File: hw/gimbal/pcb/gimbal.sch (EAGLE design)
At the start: 80 parts, among them J1 JST-XH4SMT_RA, U1 STM32F4R_64PIN, U2 TPS62172PWSON8, U3 TPS55330PQFN16, U4 MC33926, U5 DRV8313, U6 DRV8313, U7 AS5048A

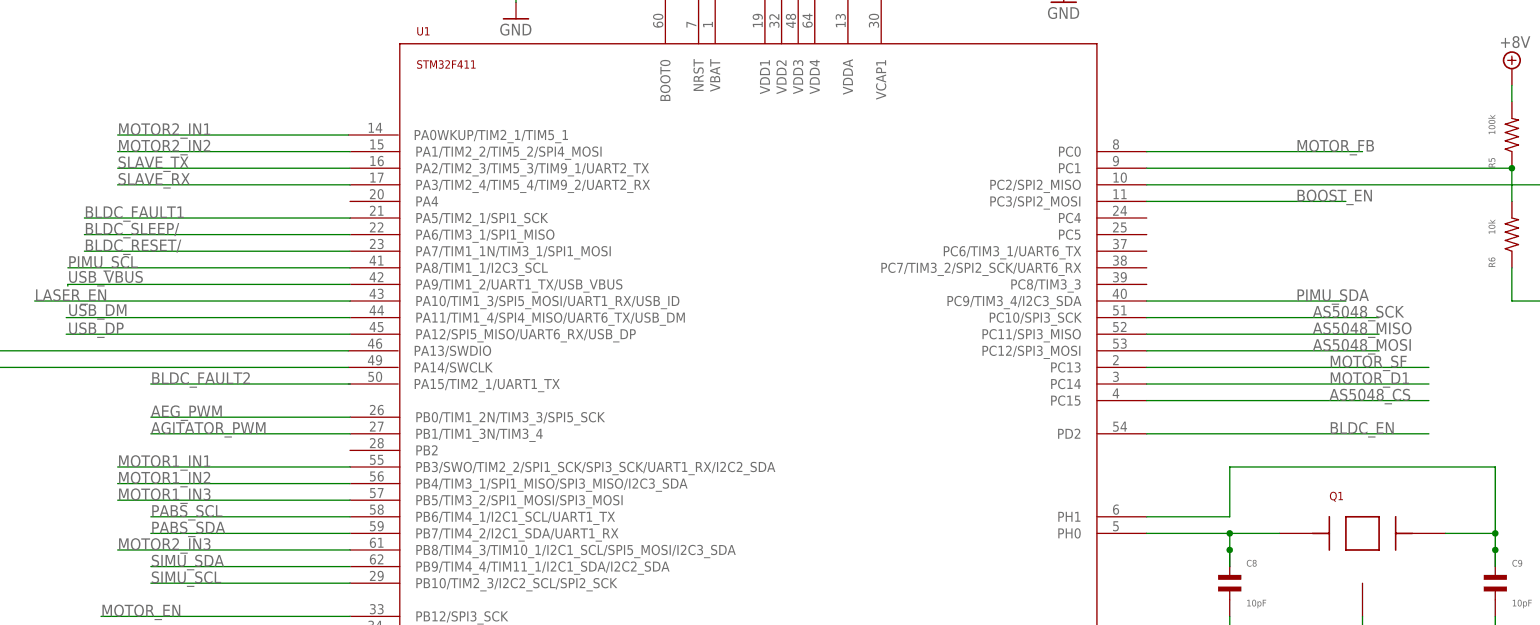
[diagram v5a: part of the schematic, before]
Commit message: gimbal: Get the board to be close to routable again, and also connect up the BLDC_FAULT2 signal, which I goofed and didn't actually connect.
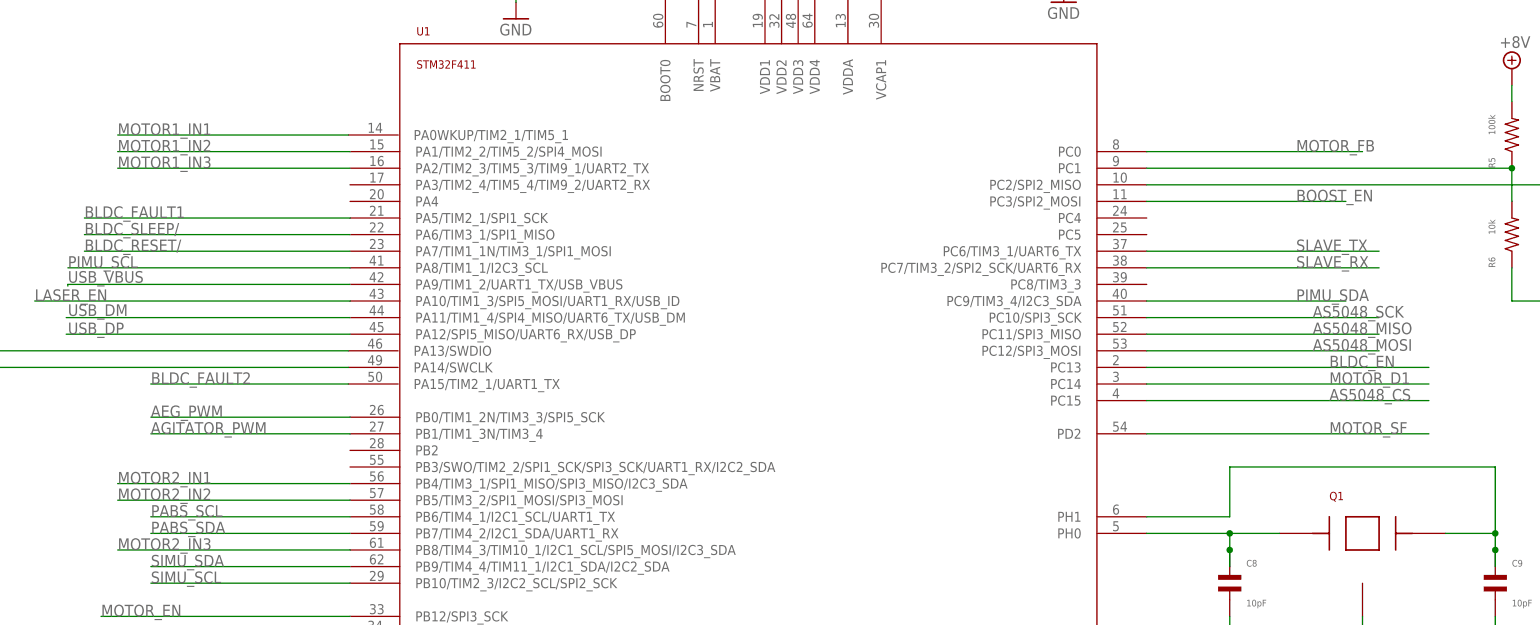
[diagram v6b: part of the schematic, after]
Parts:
- ARM: DPN 401-2002-1-ND -> 401-1999-1-ND
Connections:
- net BLDC_EN: now also U1.PC13; no longer U1.PD2
- net BLDC_FAULT2: now also U1.PA15/TIM2_1/UART1_TX
- net MOTOR1_IN1: now also U1.PA0WKUP/TIM2_1/TIM5_1; no longer U1.PB3/SWO/TIM2_2/SPI1_SCK/SPI3_SCK/UART1_RX/I2C2_SDA
- net MOTOR1_IN2: now also U1.PA1/TIM2_2/TIM5_2/SPI4_MOSI; no longer U1.PB4/TIM3_1/SPI1_MISO/SPI3_MISO/I2C3_SDA
- net MOTOR1_IN3: now also U1.PA2/TIM2_3/TIM5_3/TIM9_1/UART2_TX; no longer U1.PB5/TIM3_2/SPI1_MOSI/SPI3_MOSI
- net MOTOR2_IN1: now also U1.PB4/TIM3_1/SPI1_MISO/SPI3_MISO/I2C3_SDA; no longer U1.PA0WKUP/TIM2_1/TIM5_1
- net MOTOR2_IN2: now also U1.PB5/TIM3_2/SPI1_MOSI/SPI3_MOSI; no longer U1.PA1/TIM2_2/TIM5_2/SPI4_MOSI
- net MOTOR_SF: now also U1.PD2; no longer U1.PC13
- net SLAVE_RX: now also U1.PC7/TIM3_2/SPI2_SCK/UART6_RX; no longer U1.PA3/TIM2_4/TIM5_4/TIM9_2/UART2_RX
- net SLAVE_TX: now also U1.PC6/TIM3_1/UART6_TX; no longer U1.PA2/TIM2_3/TIM5_3/TIM9_1/UART2_TX
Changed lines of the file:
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@@
 </part>
 <part name="ARM" library="gimbal" deviceset="SLIDE_SWITCH" device="JS_SUB_SWITCH">
-<attribute name="DPN" value="401-2002-1-ND"/>
+<attribute name="DPN" value="401-1999-1-ND"/>
 </part>
 <part name="GND19" library="supply1" deviceset="GND" device=""/>
@@
 </segment>
 <segment>
-<pinref part="U1" gate="G$1" pin="PC13"/>
-<wire x1="170.18" y1="190.5" x2="213.36" y2="190.5" width="0.1524" layer="91"/>
-<label x="198.12" y="190.5" size="1.778" layer="95"/>
+<pinref part="U1" gate="G$1" pin="PD2"/>
+<wire x1="170.18" y1="180.34" x2="213.36" y2="180.34" width="0.1524" layer="91"/>
+<label x="198.12" y="180.34" size="1.778" layer="95"/>
 </segment>
 </net>
@@
 </segment>
 <segment>
-<pinref part="U1" gate="G$1" pin="PA2/TIM2_3/TIM5_3/TIM9_1/UART2_TX"/>
-<wire x1="48.26" y1="220.98" x2="12.7" y2="220.98" width="0.1524" layer="91"/>
-<label x="12.7" y="220.98" size="1.778" layer="95"/>
+<pinref part="U1" gate="G$1" pin="PC6/TIM3_1/UART6_TX"/>
+<wire x1="170.18" y1="208.28" x2="205.74" y2="208.28" width="0.1524" layer="91"/>
+<label x="193.04" y="208.28" size="1.778" layer="95"/>
 </segment>
 </net>
@@
 </segment>
 <segment>
-<pinref part="U1" gate="G$1" pin="PA3/TIM2_4/TIM5_4/TIM9_2/UART2_RX"/>
-<wire x1="48.26" y1="218.44" x2="12.7" y2="218.44" width="0.1524" layer="91"/>
-<label x="12.7" y="218.44" size="1.778" layer="95"/>
+<pinref part="U1" gate="G$1" pin="PC7/TIM3_2/SPI2_SCK/UART6_RX"/>
+<wire x1="170.18" y1="205.74" x2="205.74" y2="205.74" width="0.1524" layer="91"/>
+<label x="193.04" y="205.74" size="1.778" layer="95"/>
 </segment>
 </net>
@@
 </segment>
 <segment>
-<wire x1="48.26" y1="187.96" x2="17.78" y2="187.96" width="0.1524" layer="91"/>
+<wire x1="48.006" y1="187.96" x2="17.78" y2="187.96" width="0.1524" layer="91"/>
 <label x="17.78" y="187.96" size="1.778" layer="95"/>
+<pinref part="U1" gate="G$1" pin="PA15/TIM2_1/UART1_TX"/>
 </segment>
 </net>
@@
 </segment>
 <segment>
-<pinref part="U1" gate="G$1" pin="PB3/SWO/TIM2_2/SPI1_SCK/SPI3_SCK/UART1_RX/I2C2_SDA"/>
-<wire x1="48.26" y1="175.26" x2="12.7" y2="175.26" width="0.1524" layer="91"/>
-<label x="12.7" y="175.26" size="1.778" layer="95"/>
+<wire x1="48.006" y1="226.06" x2="12.7" y2="226.06" width="0.1524" layer="91"/>
+<label x="12.7" y="226.06" size="1.778" layer="95"/>
+<pinref part="U1" gate="G$1" pin="PA0WKUP/TIM2_1/TIM5_1"/>
 </segment>
 </net>
@@
 </segment>
 <segment>
+<pinref part="U1" gate="G$1" pin="PA1/TIM2_2/TIM5_2/SPI4_MOSI"/>
+<wire x1="48.26" y1="223.52" x2="12.7" y2="223.52" width="0.1524" layer="91"/>
+<label x="12.7" y="223.52" size="1.778" layer="95"/>
+</segment>
+</net>
+<net name="MOTOR1_IN3" class="0">
+<segment>
+<pinref part="U5" gate="G$1" pin="IN3"/>
+<wire x1="17.78" y1="-187.96" x2="-20.32" y2="-187.96" width="0.1524" layer="91"/>
+<label x="-20.32" y="-187.96" size="1.778" layer="95"/>
+</segment>
+<segment>
+<pinref part="U1" gate="G$1" pin="PA2/TIM2_3/TIM5_3/TIM9_1/UART2_TX"/>
+<wire x1="48.26" y1="220.98" x2="12.7" y2="220.98" width="0.1524" layer="91"/>
+<label x="12.7" y="220.98" size="1.778" layer="95"/>
+</segment>
+</net>
+<net name="MOTOR2_IN1" class="0">
+<segment>
+<pinref part="U6" gate="G$1" pin="IN1"/>
+<wire x1="177.8" y1="-175.26" x2="139.7" y2="-175.26" width="0.1524" layer="91"/>
+<label x="139.7" y="-175.26" size="1.778" layer="95"/>
+</segment>
+<segment>
 <pinref part="U1" gate="G$1" pin="PB4/TIM3_1/SPI1_MISO/SPI3_MISO/I2C3_SDA"/>
 <wire x1="48.26" y1="172.72" x2="12.7" y2="172.72" width="0.1524" layer="91"/>
@@
 </segment>
 </net>
-<net name="MOTOR1_IN3" class="0">
-<segment>
-<pinref part="U5" gate="G$1" pin="IN3"/>
-<wire x1="17.78" y1="-187.96" x2="-20.32" y2="-187.96" width="0.1524" layer="91"/>
-<label x="-20.32" y="-187.96" size="1.778" layer="95"/>
+<net name="MOTOR2_IN2" class="0">
+<segment>
+<pinref part="U6" gate="G$1" pin="IN2"/>
+<wire x1="177.8" y1="-182.88" x2="139.7" y2="-182.88" width="0.1524" layer="91"/>
+<label x="139.7" y="-182.88" size="1.778" layer="95"/>
 </segment>
 <segment>
@@
 <wire x1="48.26" y1="170.18" x2="12.7" y2="170.18" width="0.1524" layer="91"/>
 <label x="12.7" y="170.18" size="1.778" layer="95"/>
-</segment>
-</net>
-<net name="MOTOR2_IN1" class="0">
-<segment>
-<pinref part="U6" gate="G$1" pin="IN1"/>
-<wire x1="177.8" y1="-175.26" x2="139.7" y2="-175.26" width="0.1524" layer="91"/>
-<label x="139.7" y="-175.26" size="1.778" layer="95"/>
-</segment>
-<segment>
-<wire x1="48.006" y1="226.06" x2="12.7" y2="226.06" width="0.1524" layer="91"/>
-<label x="12.7" y="226.06" size="1.778" layer="95"/>
-<pinref part="U1" gate="G$1" pin="PA0WKUP/TIM2_1/TIM5_1"/>
-</segment>
-</net>
-<net name="MOTOR2_IN2" class="0">
-<segment>
-<pinref part="U6" gate="G$1" pin="IN2"/>
-<wire x1="177.8" y1="-182.88" x2="139.7" y2="-182.88" width="0.1524" layer="91"/>
-<label x="139.7" y="-182.88" size="1.778" layer="95"/>
-</segment>
-<segment>
-<pinref part="U1" gate="G$1" pin="PA1/TIM2_2/TIM5_2/SPI4_MOSI"/>
-<wire x1="48.26" y1="223.52" x2="12.7" y2="223.52" width="0.1524" layer="91"/>
-<label x="12.7" y="223.52" size="1.778" layer="95"/>
 </segment>
 </net>
@@
 </segment>
 <segment>
-<pinref part="U1" gate="G$1" pin="PD2"/>
-<wire x1="170.18" y1="180.34" x2="213.36" y2="180.34" width="0.1524" layer="91"/>
-<label x="198.12" y="180.34" size="1.778" layer="95"/>
-</segment>
-</net>
+<pinref part="U1" gate="G$1" pin="PC13"/>
+<wire x1="170.18" y1="190.5" x2="213.36" y2="190.5" width="0.1524" layer="91"/>
+<label x="198.12" y="190.5" size="1.778" layer="95"/>
+</segment>
+</net>

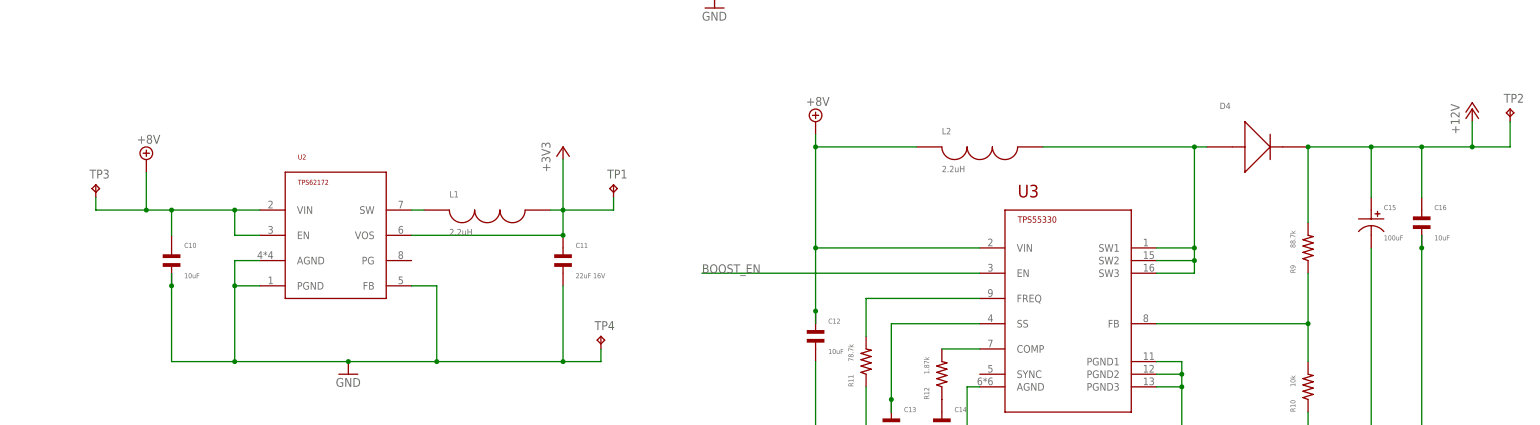
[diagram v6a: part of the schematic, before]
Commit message: gimbal: Board: Update test point names to be meaningful, and fix labels on weapon connector.
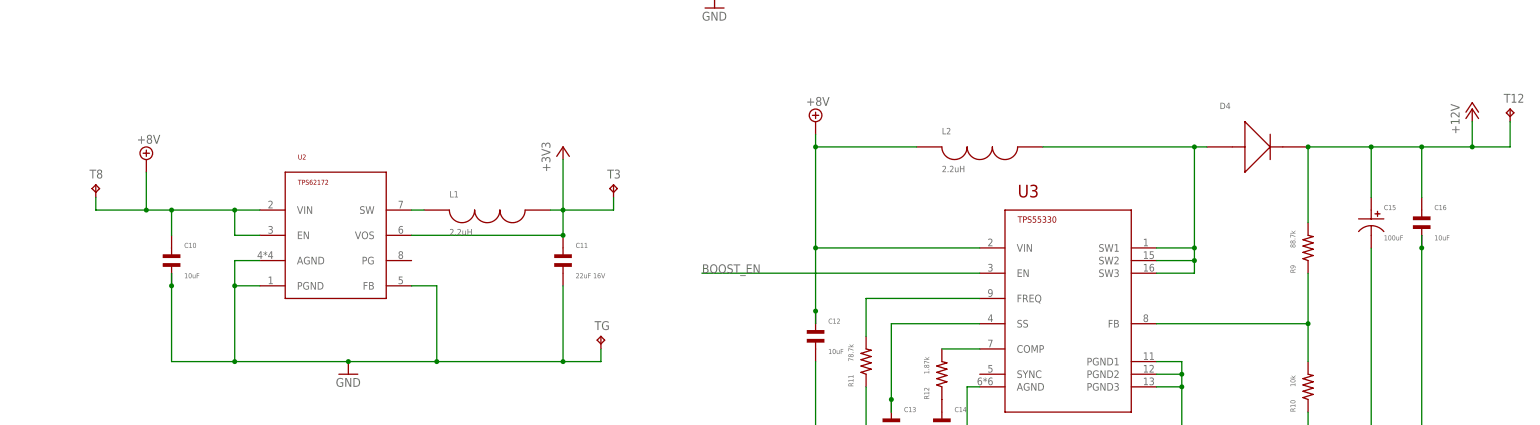
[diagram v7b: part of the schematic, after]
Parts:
- renumbered TP1 to T3, TP2 to T12, TP3 to T8, TP4 to TG
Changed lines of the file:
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@@
 <attribute name="AMFPN" value="MF-RES-0603-1.69K"/>
 </part>
-<part name="TP1" library="testpad" deviceset="TP" device="PAD1-13"/>
-<part name="TP2" library="testpad" deviceset="TP" device="PAD1-13"/>
-<part name="TP3" library="testpad" deviceset="TP" device="PAD1-13"/>
-<part name="TP4" library="testpad" deviceset="TP" device="PAD1-13"/>
+<part name="T3" library="testpad" deviceset="TP" device="PAD1-13"/>
+<part name="T12" library="testpad" deviceset="TP" device="PAD1-13"/>
+<part name="T8" library="testpad" deviceset="TP" device="PAD1-13"/>
+<part name="TG" library="testpad" deviceset="TP" device="PAD1-13"/>
 <part name="U8" library="mfdiscrete" deviceset="N-CHANNEL_FET" device="_SOT-23-3"/>
 <part name="C27" library="mfpassives" deviceset="CAPACITOR_NP" device="_0603" value="0.1uF">
@@
 <attribute name="AMFPN" x="35.56" y="-312.42" size="1.778" layer="96" rot="R90" display="off"/>
 </instance>
-<instance part="TP1" gate="G$1" x="83.82" y="71.12"/>
-<instance part="TP2" gate="G$1" x="264.16" y="86.36"/>
-<instance part="TP3" gate="G$1" x="-20.32" y="71.12"/>
-<instance part="TP4" gate="G$1" x="81.28" y="40.64"/>
+<instance part="T3" gate="G$1" x="83.82" y="71.12"/>
+<instance part="T12" gate="G$1" x="264.16" y="86.36"/>
+<instance part="T8" gate="G$1" x="-20.32" y="71.12"/>
+<instance part="TG" gate="G$1" x="81.28" y="40.64"/>
 <instance part="U8" gate="G$1" x="203.2" y="-63.5"/>
 <instance part="C27" gate="G$1" x="58.42" y="-325.12">
@@
 <pinref part="C11" gate="G$1" pin="P$2"/>
 <wire x1="73.66" y1="35.56" x2="73.66" y2="50.8" width="0.1524" layer="91"/>
-<pinref part="TP4" gate="G$1" pin="TP"/>
+<pinref part="TG" gate="G$1" pin="TP"/>
 <wire x1="73.66" y1="35.56" x2="81.28" y2="35.56" width="0.1524" layer="91"/>
 <wire x1="81.28" y1="35.56" x2="81.28" y2="38.1" width="0.1524" layer="91"/>
@@
 <pinref part="C11" gate="G$1" pin="P$1"/>
 <junction x="73.66" y="60.96"/>
-<pinref part="TP1" gate="G$1" pin="TP"/>
+<pinref part="T3" gate="G$1" pin="TP"/>
 <wire x1="73.66" y1="66.04" x2="83.82" y2="66.04" width="0.1524" layer="91"/>
 <wire x1="83.82" y1="66.04" x2="83.82" y2="68.58" width="0.1524" layer="91"/>
@@
 <junction x="-5.08" y="66.04"/>
 <pinref part="C10" gate="G$1" pin="P$1"/>
-<pinref part="TP3" gate="G$1" pin="TP"/>
+<pinref part="T8" gate="G$1" pin="TP"/>
 <wire x1="-20.32" y1="68.58" x2="-20.32" y2="66.04" width="0.1524" layer="91"/>
 <wire x1="-20.32" y1="66.04" x2="-10.16" y2="66.04" width="0.1524" layer="91"/>
@@
 <junction x="223.52" y="78.74"/>
 <pinref part="C16" gate="G$1" pin="P$1"/>
-<pinref part="TP2" gate="G$1" pin="TP"/>
+<pinref part="T12" gate="G$1" pin="TP"/>
 <wire x1="256.54" y1="78.74" x2="264.16" y2="78.74" width="0.1524" layer="91"/>
 <wire x1="264.16" y1="78.74" x2="264.16" y2="83.82" width="0.1524" layer="91"/>

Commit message: gimbal: Add manufacturer part numbers to all parts on the board.
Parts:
- ARM: AMFPN (none) -> JS102011SAQN
- C1, C7: AMFPN (none) -> CC0603KRX5R6BB475
- C11, C17, C18, C19: AMFPN (none) -> C3225X7R1C226M250AC
- C13: AMFPN (none) -> GRM188R71E473KA01D
- D4: AMFPN (none) -> B520C-13-F
- J1: AMFPN (none) -> S4B-XH-SM4-TB(LF)(SN)
- L1: AMFPN (none) -> LQH3NPN2R2MJ0L
- L2: AMFPN (none) -> ASPI-6045S-2R2N-T
- PABS, PI, SIMU: AMFPN (none) -> B4B-ZR-SM4-TF(LF)(SN)
- PGM: AMFPN (none) -> B6B-PH-K-S(LF)(SN)
- Q1: AMFPN (none) -> ABM3B-8.000MHZ-10-1-U-T
- R10: AMFPN (none) -> P10.0KHCT-ND
- R11: AMFPN (none) -> ERJ-3EKF7872V
- R12: AMFPN (none) -> ERJ-3EKF1871V
- R13, R5, R7: AMFPN (none) -> ERJ-3EKF1003V
- R14: AMFPN (none) -> ERJ-3EKF2200V
- R6, R8: AMFPN (none) -> ERJ-3EKF1002V
- R9: AMFPN (none) -> ERJ-3EKF8872V
- U1: AMFPN (none) -> STM32F411RET6
- U2: AMFPN (none) -> TPS62172DSGT
- U3: AMFPN (none) -> TPS55330RTET
- U4: AMFPN (none) -> MC33926PNBR2
- U5, U6: AMFPN (none) -> DRV8313PWP
- U7: AMFPN (none) -> AS5048A-HTSP-500
- U8: AMFPN (none) -> MF-DSC-SOT233-BSS138
- USB: AMFPN (none) -> 10118194-0001LF
- USBI: AMFPN (none) -> S4B-PH-SM4-TB(LF)(SN)
- USBO: AMFPN (none) -> B4B-PH-SM4-TB(LF)(SN)
